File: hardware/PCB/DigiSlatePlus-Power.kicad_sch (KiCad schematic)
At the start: 38 parts, among them J3 +8-24 Volt, J4 Battery, Q3 FS8205A, SW7 SW_DPDT_x2, U21 LM2596S-ADJ, U22 DW01A, U23 TP4056, U24 KA78M05_TO252, U25 LD1117S33TR_SOT223

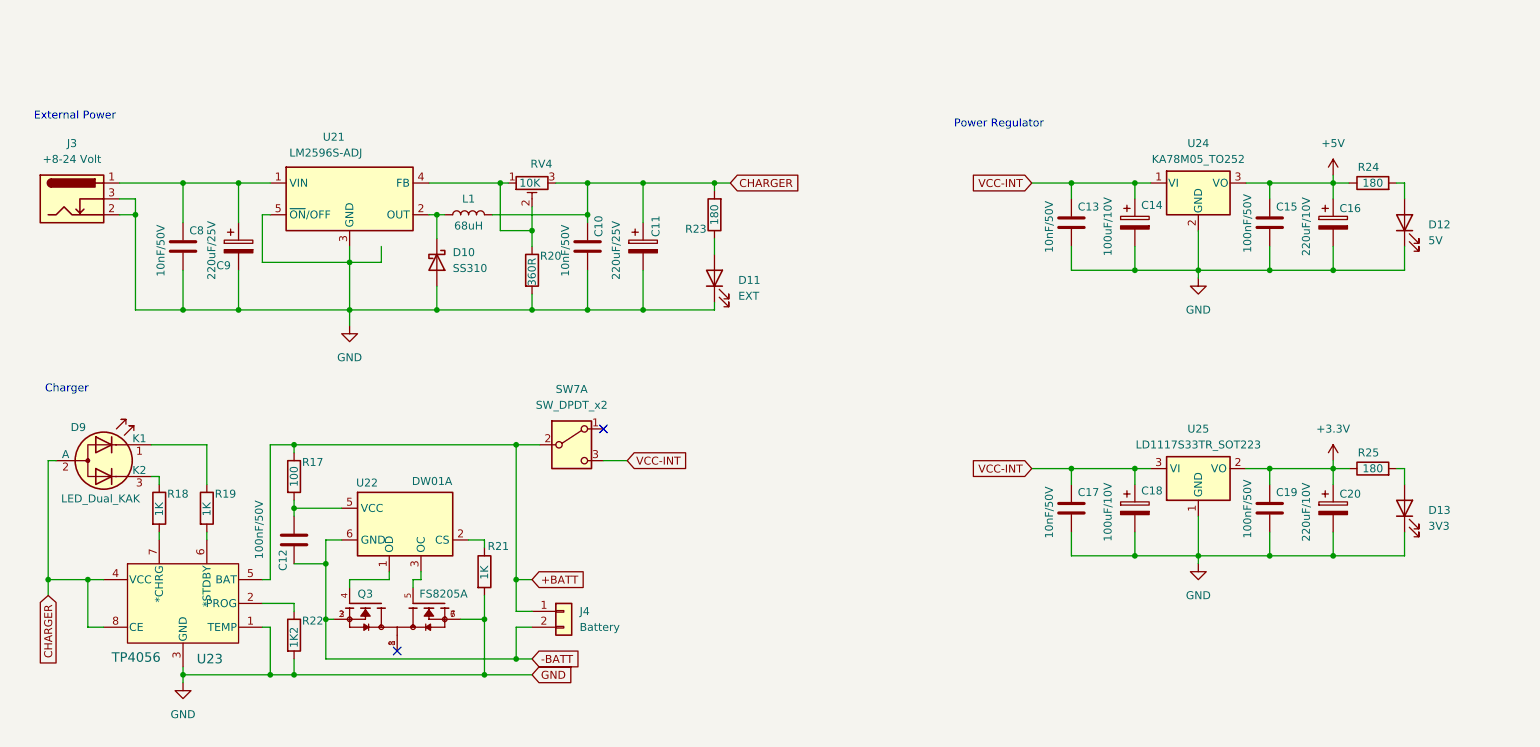
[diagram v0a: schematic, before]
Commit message: added KiCad libraries schematic bugfixes
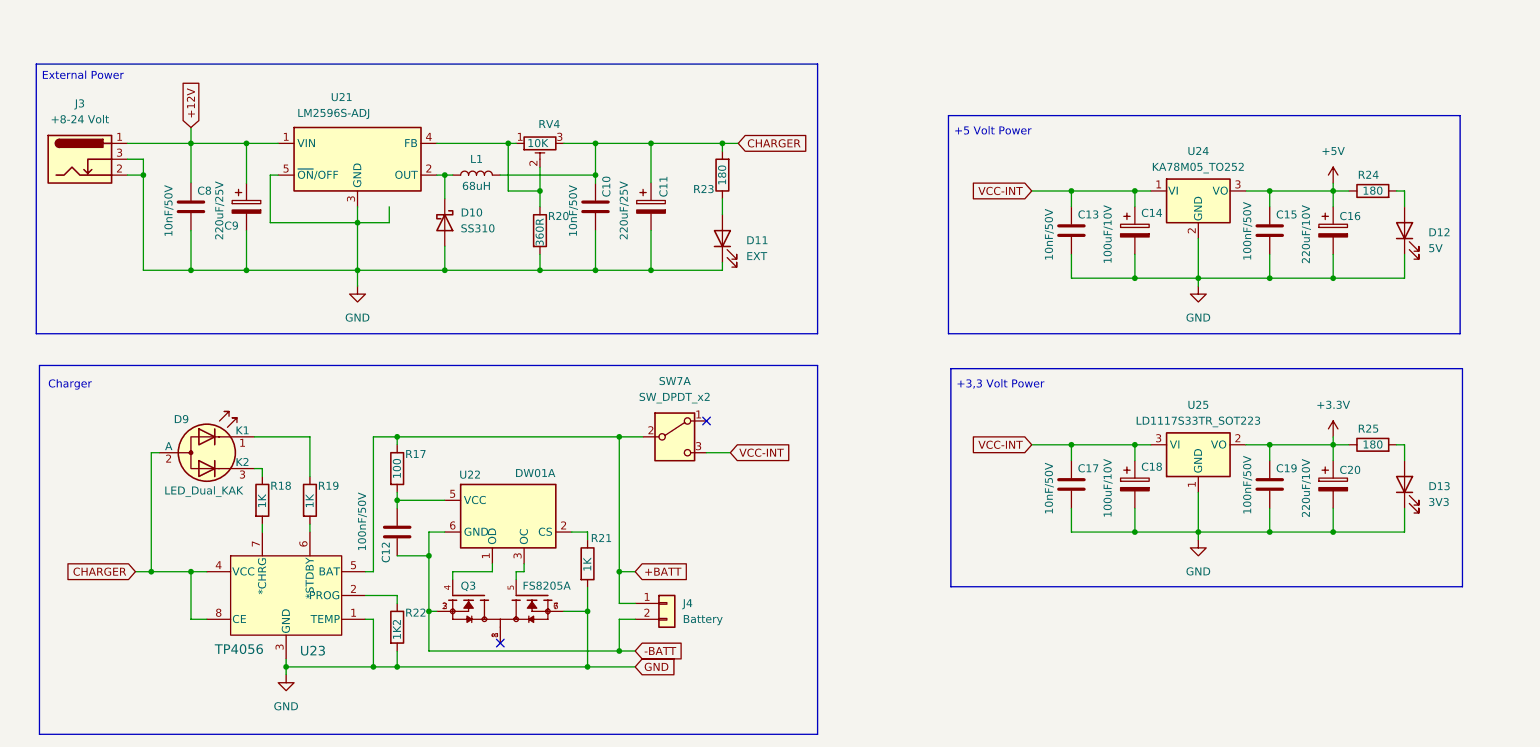
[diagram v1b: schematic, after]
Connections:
- net +12V: now reaches C8.1, C9.1, J3.1, U21.1 (VIN)
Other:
- note added: "+3,3 Volt Power"
- note added: "+5 Volt Power"
- note removed: "Power Regulator"
- moved on the sheet: C10, C11, C12, C13, C14, C15, C16, C17, C18, C19, C20, C8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

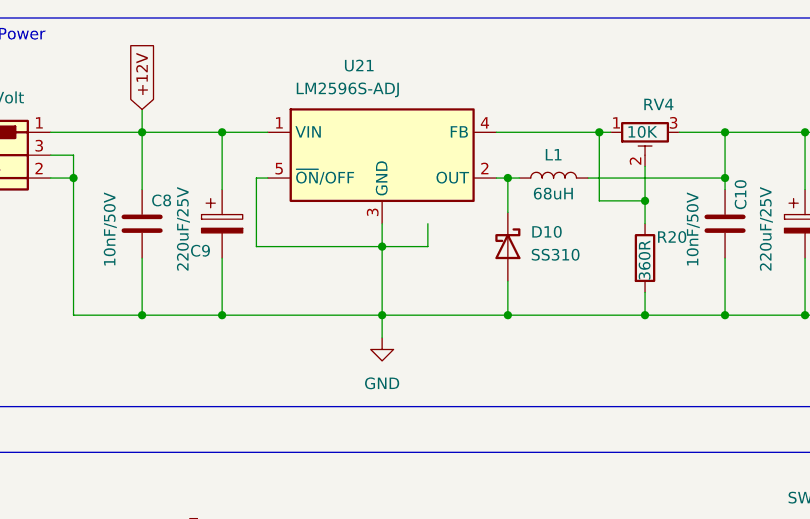
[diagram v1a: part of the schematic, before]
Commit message: minor bugfixes in schematics and board
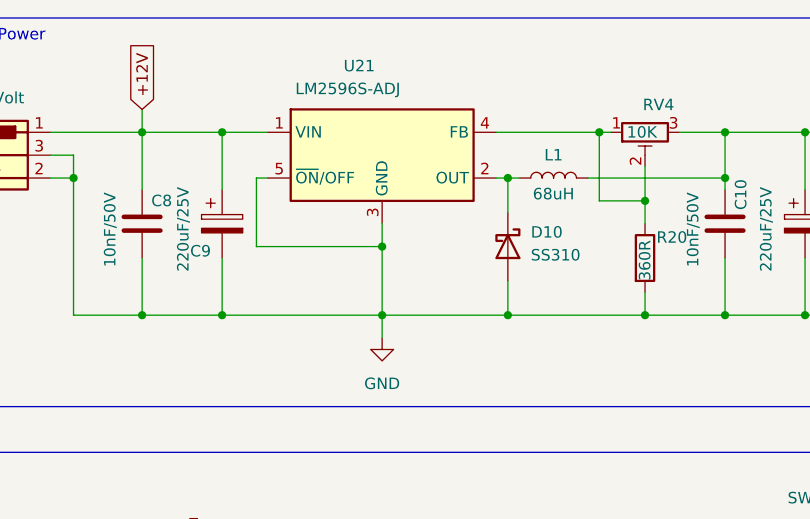
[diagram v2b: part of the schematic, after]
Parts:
- J3: footprint Connector_BarrelJack:BarrelJack_GCT_DCJ200-10-A_Horizontal -> barrel jack:DC_Power_Jack_PCB_Mounted_2.1mm
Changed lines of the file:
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@@
-	(wire
-		(pts
-			(xy 87.63 76.2) (xy 82.55 76.2)
-		)
-		(stroke
-			(width 0)
-			(type default)
-		)
-	)
 	(wire
 		(pts
@@
 		(pts
 			(xy 55.88 83.82) (xy 64.77 83.82)
-		)
-		(stroke
-			(width 0)
-			(type default)
-		)
-	)
-	(wire
-		(pts
-			(xy 87.63 73.66) (xy 87.63 76.2)
 		)
 		(stroke
@@
 				(justify left)
 				(hide yes)
-			)
-		)
-	)
-	(netclass_flag ""
-		(length 2.54)
-		(shape round)
-		(at 64.77 63.5 0)
-		(fields_autoplaced yes)
-		(effects
-			(font
-				(size 1.27 1.27)
-			)
-			(justify left bottom)
-		)
-		(property "Netclass" "Power"
-			(at 65.4685 60.96 0)
-			(effects
-				(font
-					(size 1.27 1.27)
-					(italic yes)
-				)
-				(justify left)
-			)
-		)
-	)
-	(netclass_flag ""
-		(length 2.54)
-		(shape round)
-		(at 228.6 71.12 0)
-		(fields_autoplaced yes)
-		(effects
-			(font
-				(size 1.27 1.27)
-			)
-			(justify left bottom)
-		)
-		(property "Netclass" "Power"
-			(at 229.2985 68.58 0)
-			(effects
-				(font
-					(size 1.27 1.27)
-					(italic yes)
-				)
-				(justify left)
-			)
-		)
-	)
-	(netclass_flag ""
-		(length 2.54)
-		(shape round)
-		(at 196.85 71.12 0)
-		(fields_autoplaced yes)
-		(effects
-			(font
-				(size 1.27 1.27)
-			)
-			(justify left bottom)
-		)
-		(property "Netclass" "Power"
-			(at 197.5485 68.58 0)
-			(effects
-				(font
-					(size 1.27 1.27)
-					(italic yes)
-				)
-				(justify left)
 			)
 		)
@@
 		(property "Netclass" "Power"
 			(at 89.5985 149.86 0)
-			(effects
-				(font
-					(size 1.27 1.27)
-					(italic yes)
-				)
-				(justify left)
-			)
-		)
-	)
-	(netclass_flag ""
-		(length 2.54)
-		(shape round)
-		(at 140.97 63.5 0)
-		(fields_autoplaced yes)
-		(effects
-			(font
-				(size 1.27 1.27)
-			)
-			(justify left bottom)
-		)
-		(property "Netclass" "Power"
-			(at 141.6685 60.96 0)
 			(effects
 				(font
@@
 			)
 		)
-		(property "Footprint" "Connector_BarrelJack:BarrelJack_GCT_DCJ200-10-A_Horizontal"
+		(property "Footprint" "barrel jack:DC_Power_Jack_PCB_Mounted_2.1mm"
 			(at 39.37 67.056 0)
 			(effects

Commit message: new harware bugfixes while building the prototype
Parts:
- added C36, C38: 10nF/50V, Capacitor_SMD:C_1206_3216Metric_Pad1.33x1.80mm_HandSolder, symbol Device:C
- added C37: 100uF/10V, Capacitor_Tantalum_SMD:CP_EIA-7343-31_Kemet-D_Pad2.25x2.55mm_HandSolder, symbol Device:C_Polarized
- added C39: 10nF/50V, Capacitor_SMD:C_0805_2012Metric_Pad1.18x1.45mm_HandSolder, symbol Device:C
- added D15: SS310, Diode_SMD:D_SMA, symbol Diode:SS310
- added L2: 68uH, Inductor_SMD:L_7.3x7.3_H3.5, symbol Device:L
- added R35, R36: 15k, Resistor_SMD:R_0805_2012Metric_Pad1.20x1.40mm_HandSolder, symbol Device:R
- added U33: MT3608, Package_TO_SOT_SMD:SOT-23-6, symbol Regulator_Switching:MT3608
- R24: value 180 -> 220
- R25: value 180 -> 120
- U23: footprint TP4056:TP4056-42-ESOP8_TPW -> TP4056:TP4056-42-SOP8_TPW_1
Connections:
- net VCC-INT renamed +6V
- net +6V: now also C38.1, C39.1, D15.1 (K), R35.2; no longer SW7.3 (C)
- new net: C36.2, C37.2, C38.2, C39.2, R36.1, U33.2 (GND)
- new net: R35.1, R36.2, U33.3 (FB)
- new net: D15.2 (A), L2.2, U33.1 (SW)
- new net SWITCHED: C36.1, C37.1, L2.1, SW7.3 (C), U33.4 (EN), U33.5 (IN)
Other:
- note added: "Battery step up converter"
- moved on the sheet: C10, C11, C12, C13, C14, C15, C16, C17, C18, C19, C20, C8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
